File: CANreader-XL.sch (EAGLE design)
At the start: 101 parts, among them IC1 MCP2551, IC2 TJA1055T/3, IC3 BD9G101G, IC4 LM1117IMPX-3.3, IC6 STM32F107RBT, IC7 DP83848I, Q1 25MHz, SW1 SLEEP, SW2 TERM, U1 HC_05, X1 MINI-USB, X2 SWD, X3 GPIO, X4 UART, X5 CAN, X6 LAN, X7 J11012F21K

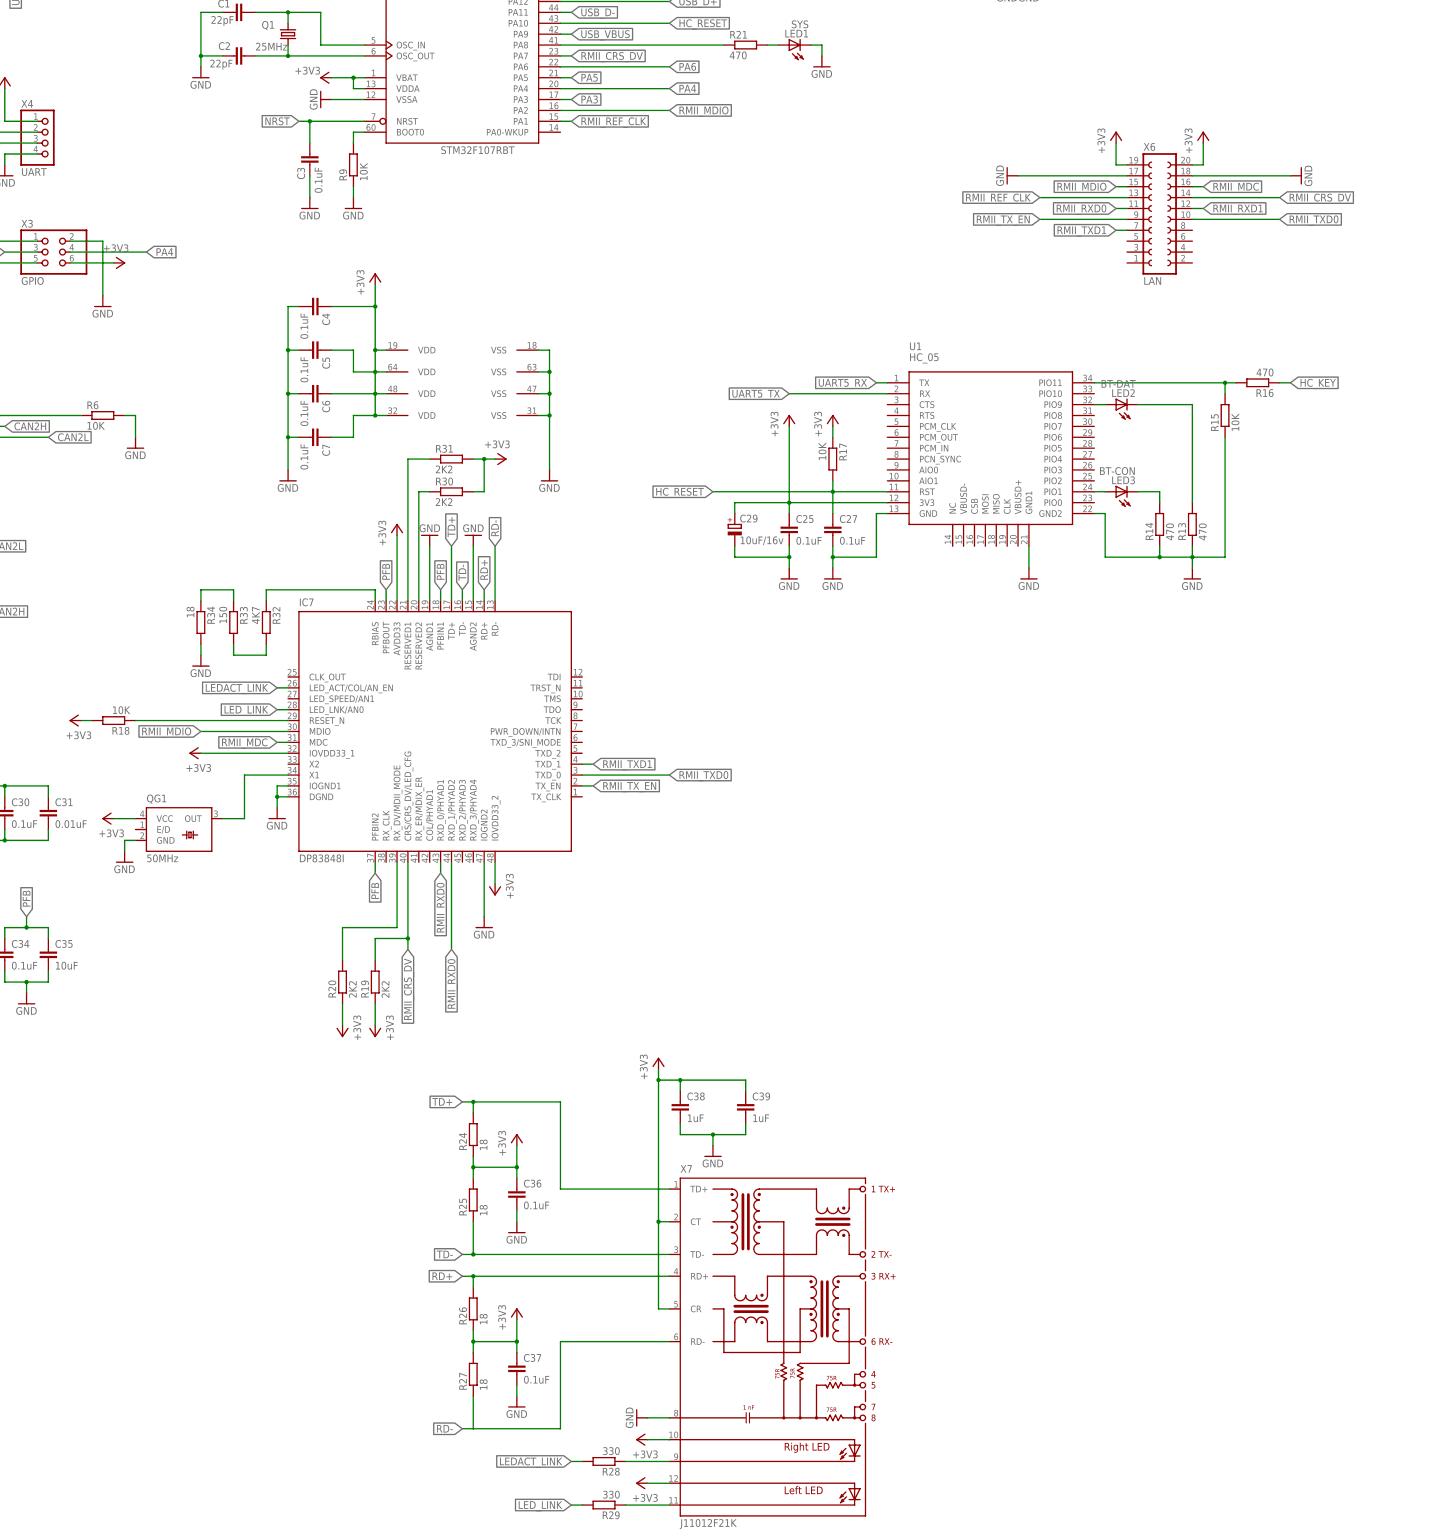
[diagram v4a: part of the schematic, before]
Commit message: RJ45 connector
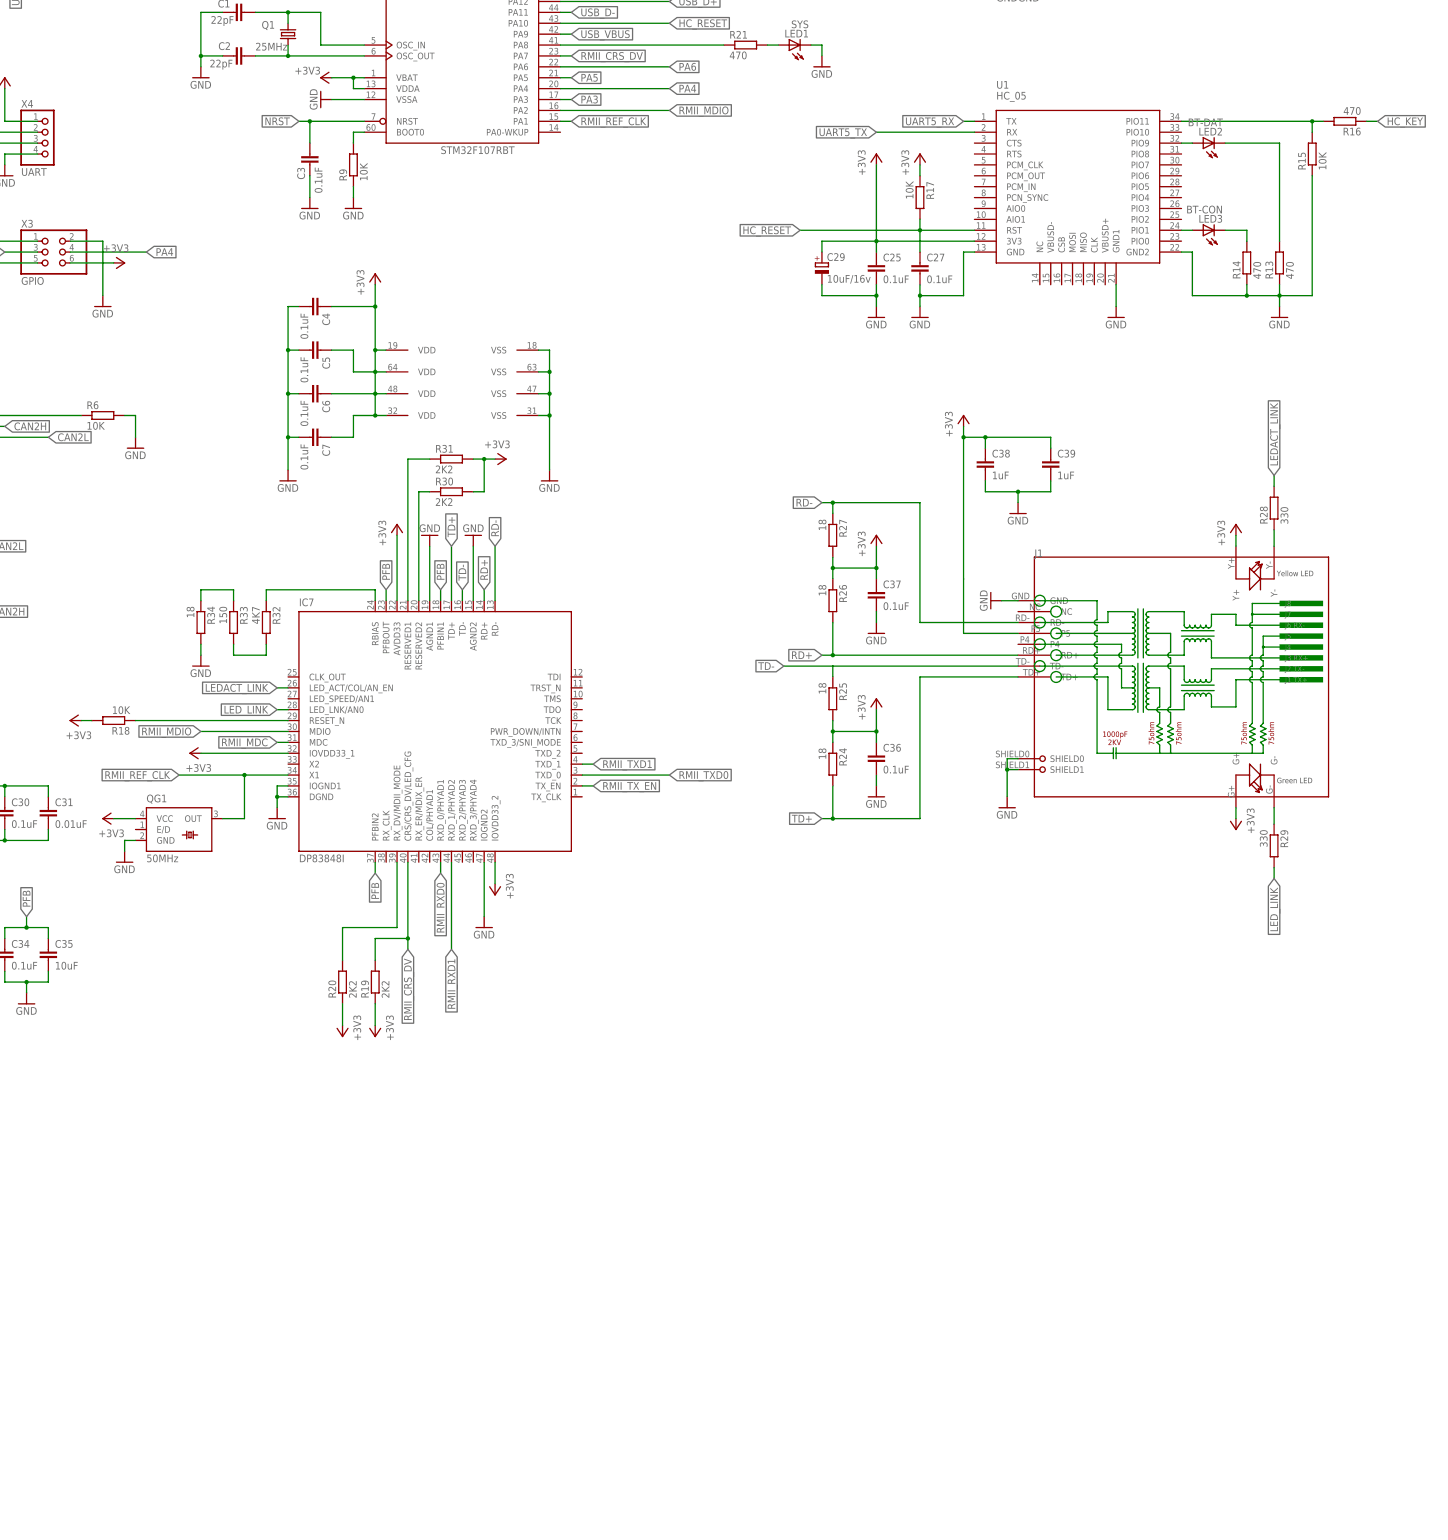
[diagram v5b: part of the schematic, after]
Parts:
- removed X6: LAN, con-lsta:FE10-2W
- removed X7: J11012F21K, con-pulse:J11012F21K
- added J1: (no value), Connector:RJ45-HR911105A-HR911105A
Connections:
- removed net N$24: IC7.X1, QG1.OUT
- new net N$29: J1.TD-
- new net N$30: J1.P5
- net +3V3: now also J1.G+, J1.Y+; no longer X6.19, X6.20, X7.A-L, X7.A-R, X7.CR, X7.CT
- net GND: now also J1.GND, J1.SHIELD0, J1.SHIELD1; no longer X6.17, X6.18, X7.8
- net N$22: now also J1.G-, R29.1; no longer R28.1, X7.C-R
- net N$23: now also J1.Y-, R28.1; no longer R29.1, X7.C-L
- net RD+: now also J1.RD+; no longer X7.RD+
- net RD-: now also J1.RD-; no longer X7.RD-
- net RMII_CRS_DV: no longer X6.14
- net RMII_MDC: no longer X6.16
- net RMII_MDIO: no longer X6.15
- net RMII_REF_CLK: now also IC7.X1, QG1.OUT; no longer X6.13
- net RMII_RXD0: no longer IC7.RXD_1/PHYAD2, X6.11
- net RMII_RXD1: now also IC7.RXD_1/PHYAD2; no longer X6.12
- net RMII_TXD0: no longer X6.10
- net RMII_TXD1: no longer X6.7
- net RMII_TX_EN: no longer X6.9
- net TD+: now also J1.TD+; no longer X7.TD+
- net TD-: no longer X7.TD-
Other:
- moved on the sheet: C25, C27, C29, C36, C37, C38, C39, LED2, LED3, R13, R14, R15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

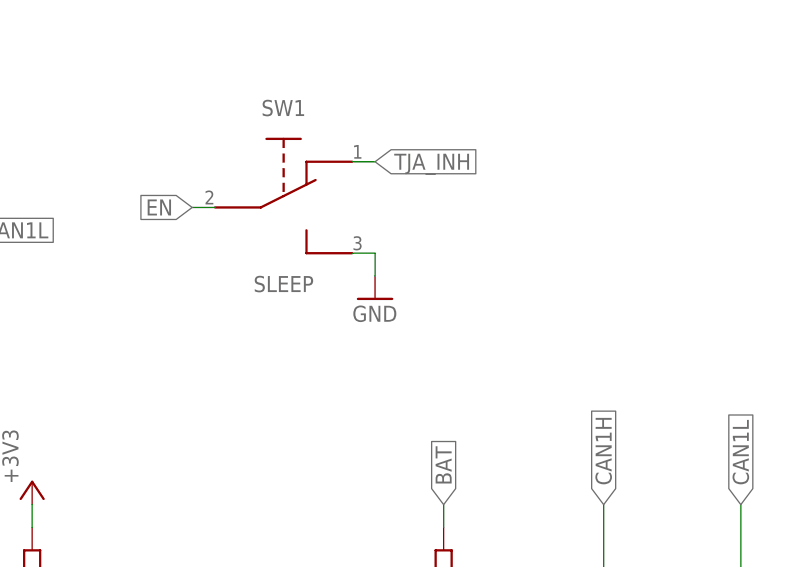
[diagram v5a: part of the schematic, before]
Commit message: fix sleep mode switch error
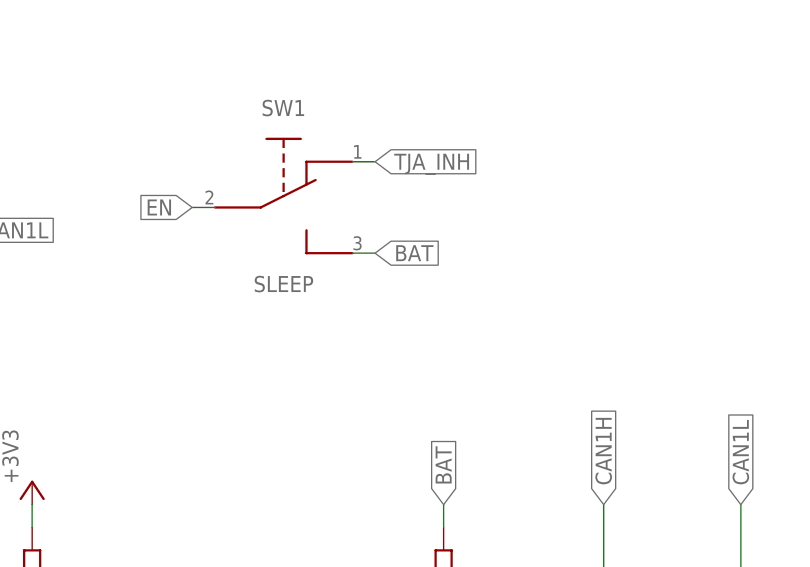
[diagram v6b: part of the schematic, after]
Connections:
- net BAT: now also SW1.3
- net GND: no longer SW1.3
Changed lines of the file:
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@@
 <part name="SW2" library="STM32_CAN-USB" deviceset="SS12F27" device="" value="TERM"/>
 <part name="SW1" library="STM32_CAN-USB" deviceset="SS12F27" device="" value="SLEEP"/>
-<part name="GND29" library="supply1" deviceset="GND" device=""/>
 <part name="R23" library="rcl" deviceset="R-EU_" device="R0805" value="3K3"/>
 <part name="+3V11" library="supply1" deviceset="+3V3" device=""/>
@@
 <instance part="SW2" gate="G$1" x="-55.88" y="-104.14"/>
 <instance part="SW1" gate="G$1" x="228.6" y="132.08"/>
-<instance part="GND29" gate="1" x="238.76" y="121.92"/>
 <instance part="R23" gate="G$1" x="190.5" y="91.44" smashed="yes" rot="R90">
 <attribute name="NAME" x="189.0014" y="87.63" size="1.778" layer="95" rot="R90"/>
@@
 </segment>
 <segment>
-<pinref part="SW1" gate="G$1" pin="3"/>
-<wire x1="236.22" y1="127" x2="238.76" y2="127" width="0.1524" layer="91"/>
-<pinref part="GND29" gate="1" pin="GND"/>
-<wire x1="238.76" y1="124.46" x2="238.76" y2="127" width="0.1524" layer="91"/>
-</segment>
-<segment>
 <pinref part="IC6" gate="MCU" pin="VSSA"/>
 <pinref part="GND36" gate="1" pin="GND"/>
@@
 <pinref part="C14" gate="G$1" pin="+"/>
 </segment>
-</net>
+<segment>
+<pinref part="SW1" gate="G$1" pin="3"/>
+<wire x1="236.22" y1="127" x2="238.76" y2="127" width="0.1524" layer="91"/>
+<label x="238.76" y="127" size="1.778" layer="95" xref="yes"/>
+</segment>
+</net>
